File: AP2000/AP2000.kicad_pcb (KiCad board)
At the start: 4 copper layers, 108 x 110 mm, 150 parts, among them IC2 TPS23751PWPR, J1 USB_OTG, J11 Barrel_Jack, J12 Bus_PCI_Express_Mini, J2 USB_OTG, J3 Boot, J9 0826-1X1T-GH-F, Q1 FDS86242, SW1 SW_SPST, U1 CH340N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

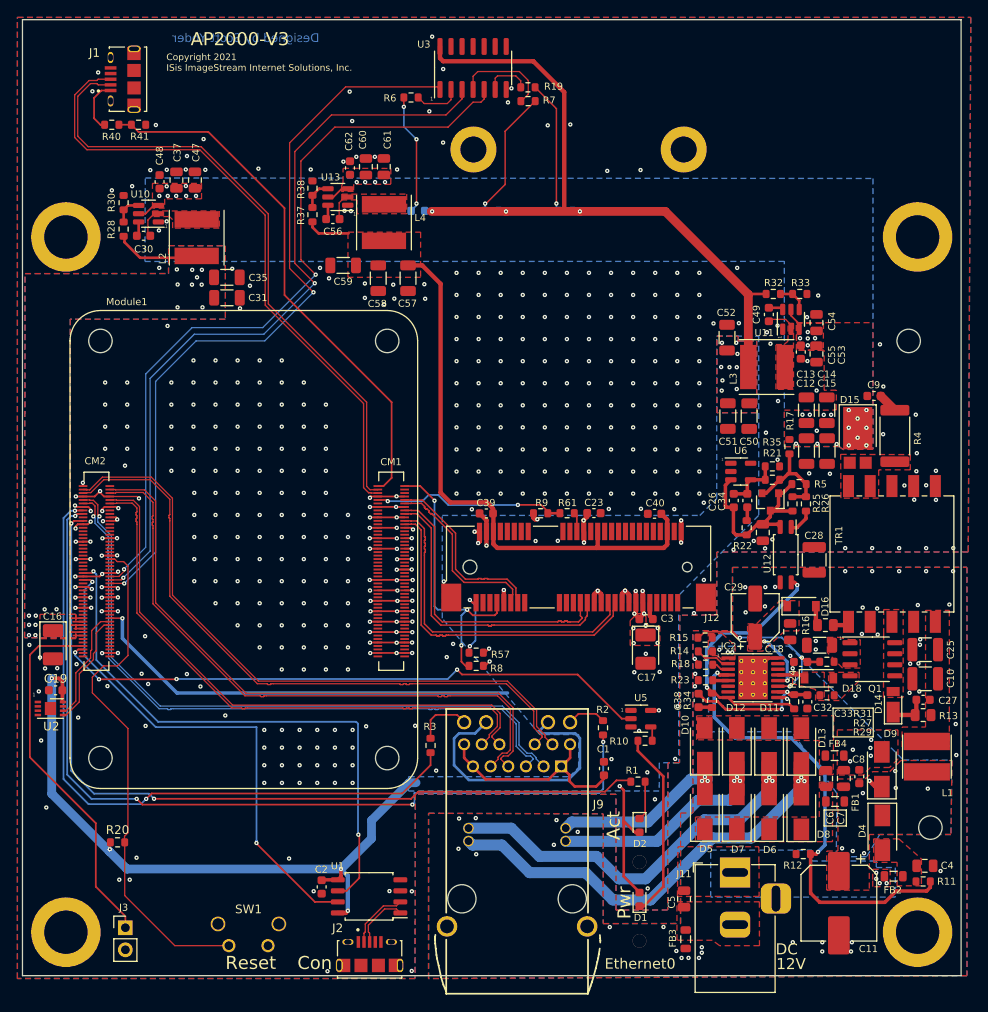
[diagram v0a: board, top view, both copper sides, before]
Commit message: Mods to AP2000 for manufacturing. 50 PCBs ordered from JLCPCB with SMd assembly.
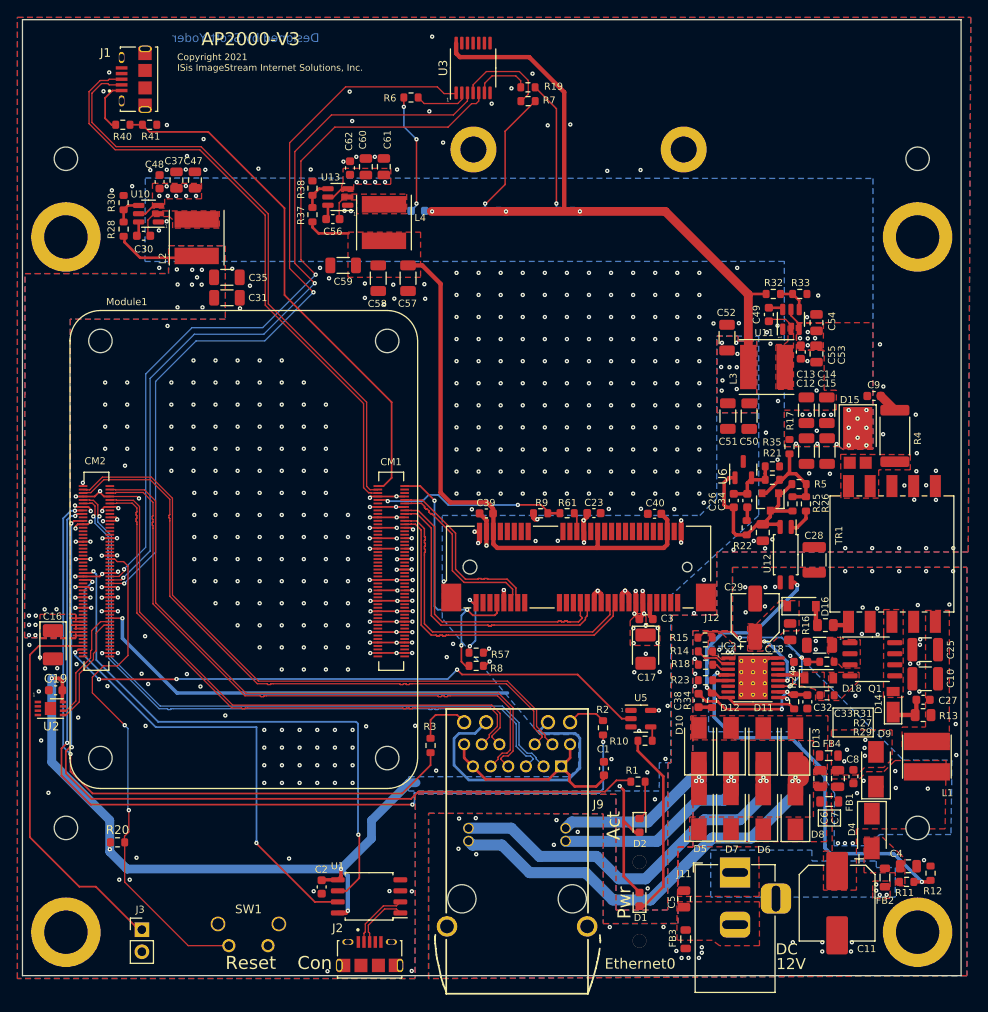
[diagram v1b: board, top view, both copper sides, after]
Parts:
- added H8: HeatSink, Scott:CM4_Mounting_Hole, F.Cu at (5.00, 93.0)
- added H9: HeatSink, Scott:CM4_Mounting_Hole, F.Cu at (103.0, 16.0)
- H1: value Mounting Hole -> HeatSink
- U3: footprint Package_SO:SOIC-14_3.9x8.7mm_P1.27mm -> Package_SO:TSSOP-14_4.4x5mm_P0.65mm
- U6: footprint Package_TO_SOT_SMD:SOT-23-5 -> Package_TO_SOT_SMD:SOT-23
- moved H6 99.2 mm to (5.00, 16.0)
- moved R12 14.8 mm to (104.5, 98.2), turned to 90 degrees
- moved J3 1.91 mm to (13.7, 104.7)
- moved C4 1.90 mm to (101.9, 97.4)
- moved R11 1.90 mm to (101.7, 99.2)
- moved H7 1.47 mm to (103.0, 93.0)
- moved J1 1.27 mm to (14.1, 6.85)
- moved R40 1.27 mm to (11.5, 12.1)
- moved R41 1.27 mm to (14.6, 12.1)
- moved D4 1.22 mm to (97.7, 93.4)
- moved FB2 1.01 mm to (99.2, 98.7), turned to 90 degrees
- moved C8 0.67 mm to (95.6, 87.1)
- moved C6 0.67 mm to (91.8, 87.3)
- moved C7 0.67 mm to (93.8, 87.3)
- moved D10 0.67 mm to (77.8, 83.5)
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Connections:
- U6 pad 1: (no net) -> Net-(C26-Pad1)
- U6 pad 2: (no net) -> Net-(C26-Pad2)
- U6 pad 3: Net-(C26-Pad1) -> GND
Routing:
- net /PoE/APD: track 52.6 -> 45.5 mm
- net /CM4_HighSpeed/USBD_P: track 73.2 -> 70.5 mm
- net /CM4_HighSpeed/USBD_N: track 72.0 -> 69.3 mm
- net Net-(J3-Pad1): track 42.5 -> 44.8 mm
- net /CM4_GPIO ( Ethernet, GPIO, SDCARD)/GPIO2: track 87.3 -> 89.3 mm
- net /CM4_GPIO ( Ethernet, GPIO, SDCARD)/E0_LEDG: track 79.4 -> 77.4 mm
- net /+3.3v: track 281.8 -> 280.0 mm
- net Net-(Module1-Pad101): track 61.2 -> 59.9 mm
- net Net-(R19-Pad1): track 5.34 -> 6.61 mm
- net Net-(Module1-Pad21): track 96.6 -> 97.8 mm
- net /CM4_GPIO ( Ethernet, GPIO, SDCARD)/E0_LEDY: track 102.1 -> 103.1 mm
- net Net-(C26-Pad1): track 22.4 -> 23.4 mm
- net /PoE/VDD: track 1.70 -> 0.74 mm
- net /CM4_GPIO ( Ethernet, GPIO, SDCARD)/GPIO4: track 88.9 -> 88.0 mm
- net /CM4_GPIO ( Ethernet, GPIO, SDCARD)/GPIO10: track 59.2 -> 58.4 mm, vias 0 -> 2
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
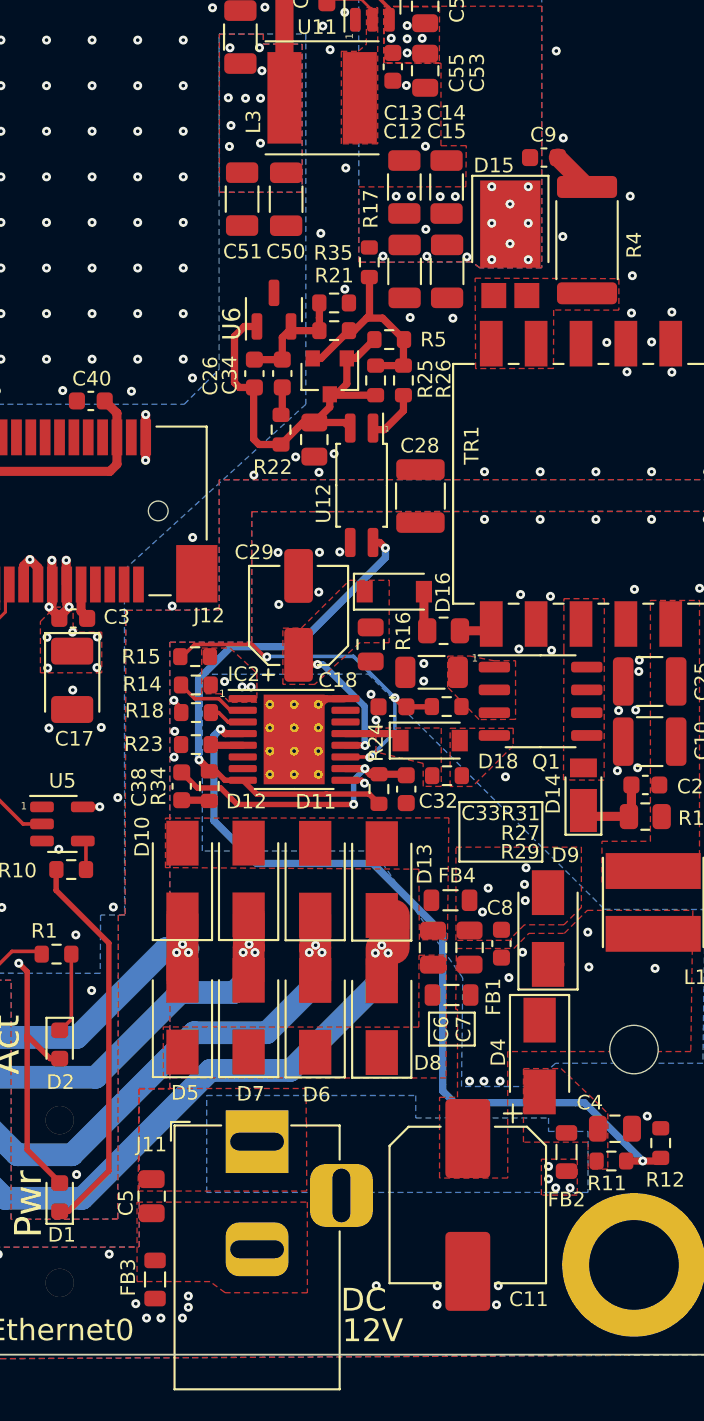
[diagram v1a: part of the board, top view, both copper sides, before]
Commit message: Fix up footprints due to changed components / out of stock components with JLCPCB
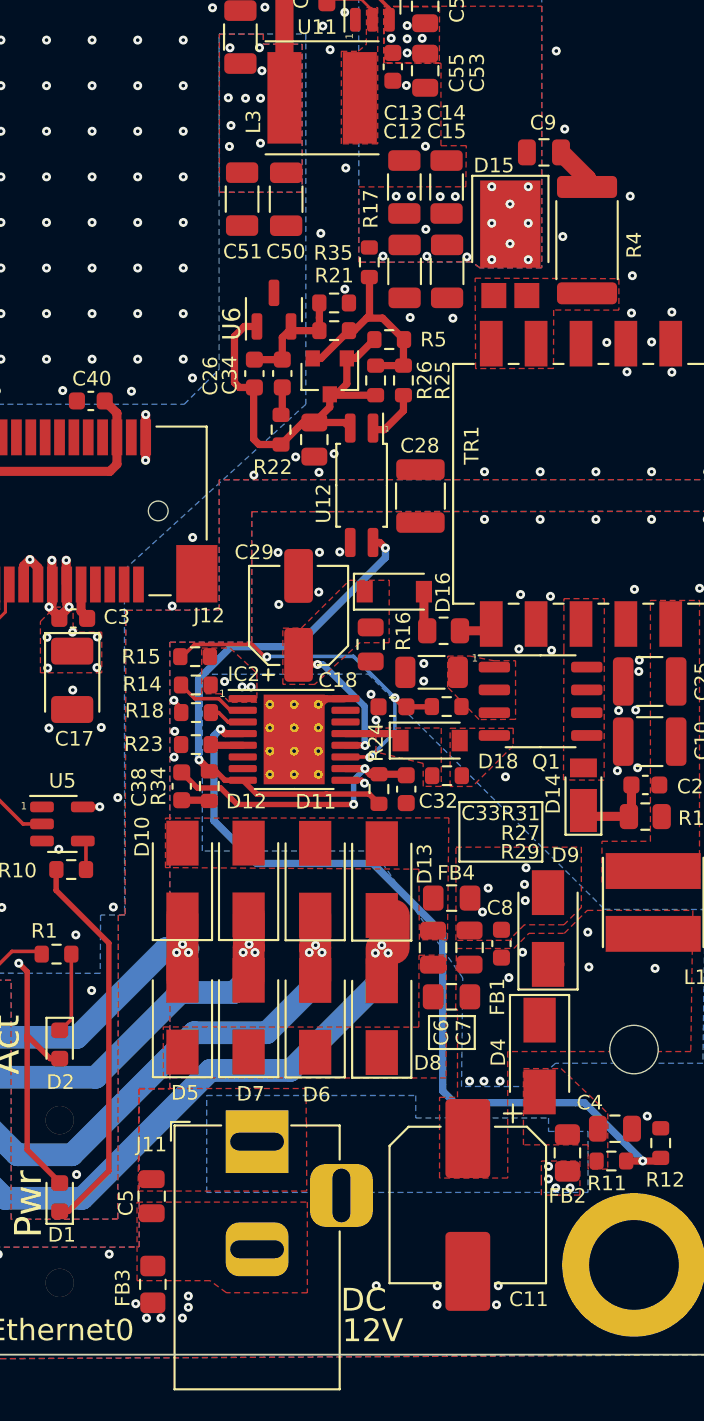
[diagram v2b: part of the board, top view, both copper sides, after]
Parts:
- C9: footprint Capacitor_SMD:C_0603_1608Metric -> Capacitor_SMD:C_0805_2012Metric
- FB1, FB2, FB3, FB4: footprint Inductor_SMD:L_0805_2012Metric -> Inductor_SMD:L_0805_2012Metric_Pad1.15x1.40mm_HandSolder
- moved FB3 0.30 mm to (76.2, 106.1)
- moved C9 0.29 mm to (98.0, 43.0)
- moved FB4 0.14 mm to (92.8, 84.6)
- moved FB1 0.10 mm to (92.8, 90.1)
- moved FB2 0.07 mm to (99.3, 98.8)
